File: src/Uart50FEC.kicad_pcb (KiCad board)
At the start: 2 copper layers, 24 x 27.9 mm, 23 parts, among them J1 105444-0001, J2 B4B-XH-A, U1 FT232RL, U2 MIC2005A-1

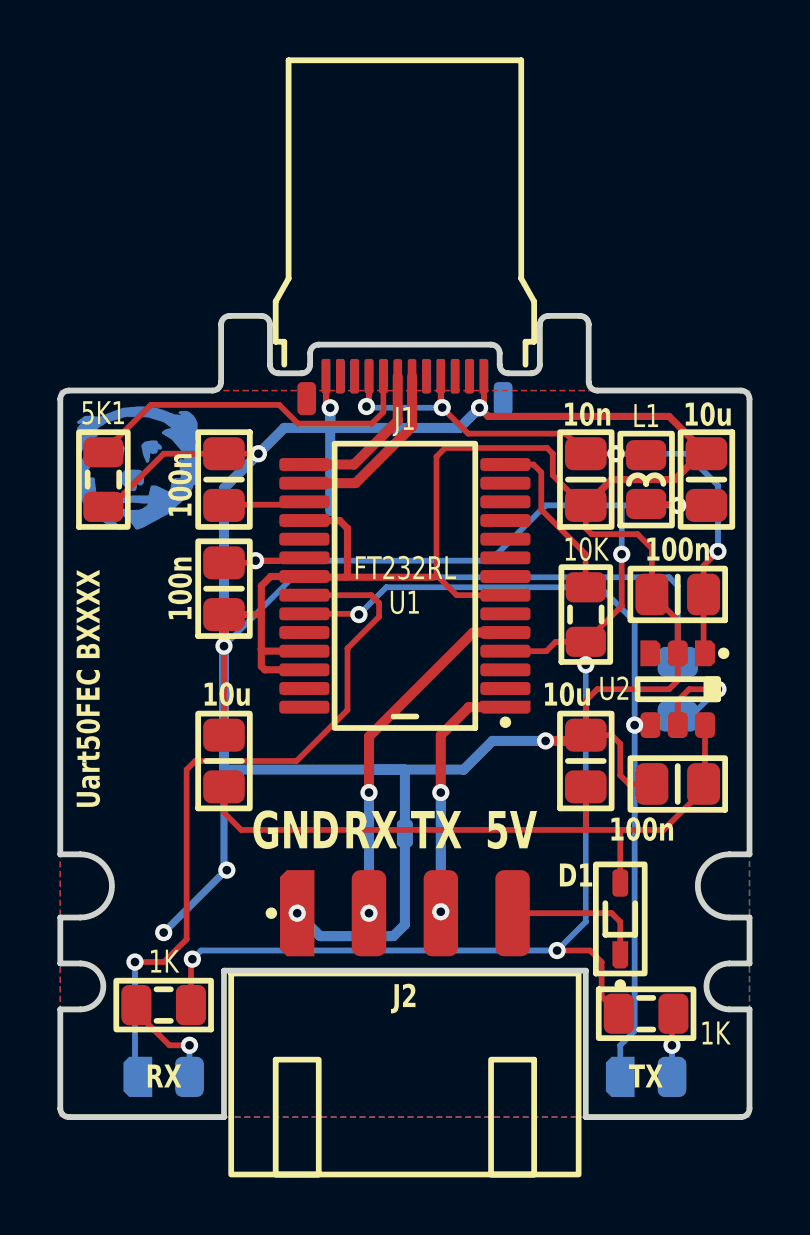
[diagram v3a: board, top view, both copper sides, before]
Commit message: Added jumper for always on
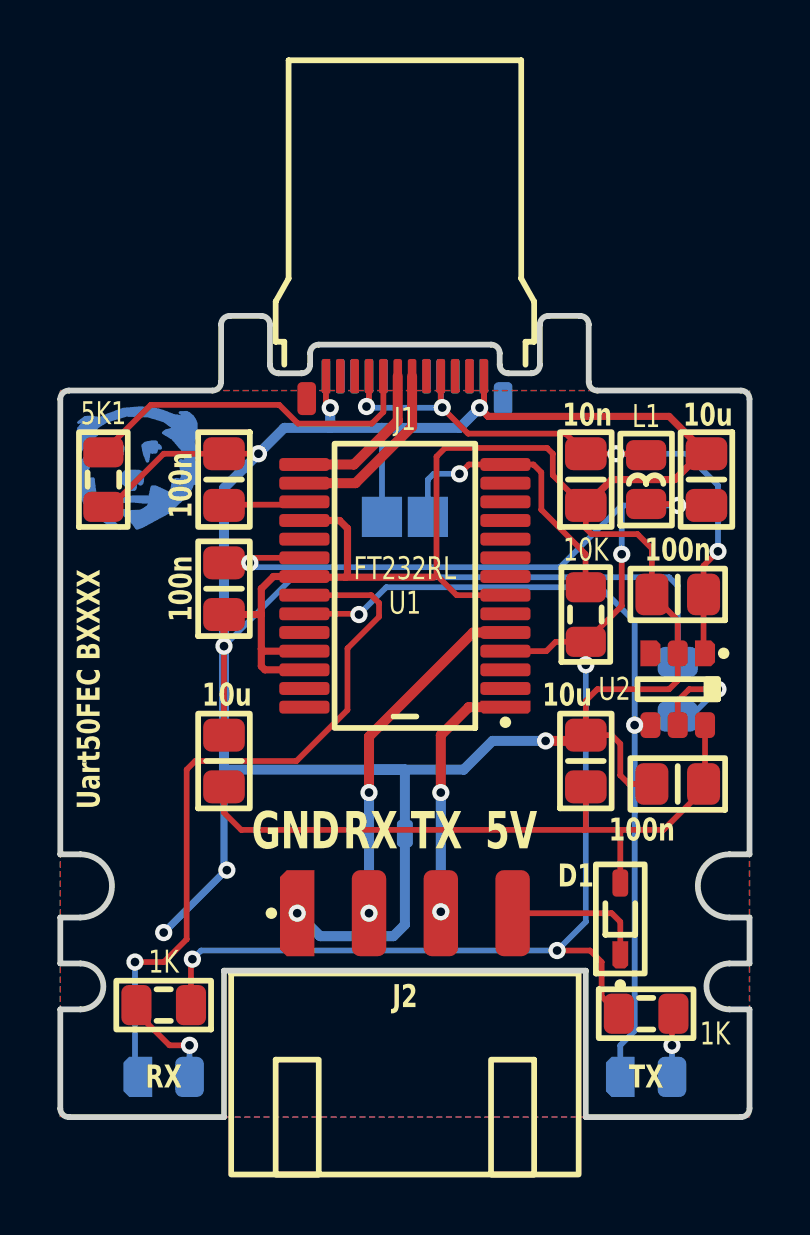
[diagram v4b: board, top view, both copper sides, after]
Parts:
- added JP1: ALWAYS ON, Medo64:JP (0805), B.Cu at (32.0, 27.0)
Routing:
- net PWREN#: track 6.00 -> 10.2 mm, vias 0 -> 1
- net GND: track 150.7 -> 150.2 mm
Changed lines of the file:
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@@
+		)
+	)
+	(footprint "Medo64:JP (0805)"
+		(layer "B.Cu")
+		(at 32 27 180)
+		(property "Reference" "JP1"
+			(at 0 1.5 180)
+			(layer "B.SilkS")
+			(hide yes)
+			(effects
+				(font
+					(size 0.8 0.6)
+					(thickness 0.15)
+					(bold yes)
+				)
+				(justify mirror)
+			)
+		)
+		(property "Value" "ALWAYS ON"
+			(at 0 -1.6 180)
+			(layer "B.SilkS")
+			(effects
+				(font
+					(size 0.8 0.6)
+					(thickness 0.15)
+					(bold yes)
+				)
+				(justify mirror)
+			)
+		)
+		(property "Footprint" "Medo64:JP (0805)"
+			(at 0 0 0)
+			(unlocked yes)
+			(layer "B.Fab")
+			(hide yes)
+			(effects
+				(font
+					(size 1.27 1.27)
+				)
+				(justify mirror)
+			)
+		)
+		(property "Datasheet" ""
+			(at 0 0 0)
+			(unlocked yes)
+			(layer "B.Fab")
+			(hide yes)
+			(effects
+				(font
+					(size 1.27 1.27)
+				)
+				(justify mirror)
+			)
+		)
+		(property "Description" ""
+			(at 0 0 0)
+			(unlocked yes)
+			(layer "B.Fab")
+			(hide yes)
+			(effects
+				(font
+					(size 1.27 1.27)
+				)
+				(justify mirror)
+			)
+		)
+		(attr smd)
+		(fp_rect
+			(start 1.65 -0.85)
+			(end -1.65 0.85)
+			(stroke
+				(width 0.2)
+				(type default)
+			)
+			(fill none)
+			(layer "B.SilkS")
+		)
+		(fp_rect
+			(start 0.1 -0.7)
+			(end -0.1 0.7)
+			(stroke
+				(width 0)
+				(type solid)
+			)
+			(fill solid)
+			(layer "B.Mask")
+		)
+		(fp_rect
+			(start 1.75 -0.95)
+			(end -1.75 0.95)
+			(stroke
+				(width 0.01)
+				(type dash)
+			)
+			(fill none)
+			(layer "B.CrtYd")
+		)
+		(pad "1" smd roundrect
+			(at -0.8 0 180)
+			(size 1.4 1.4)
+			(layers "B.Cu" "B.Mask")
+			(roundrect_rratio 0.5)
+			(chamfer_ratio 0)
+			(chamfer top_right bottom_right)
+			(net 10 "PWREN#")
+			(thermal_bridge_angle 45)
+		)
+		(pad "2" smd roundrect
+			(at 0.8 0 180)
+			(size 1.4 1.4)
+			(layers "B.Cu" "B.Mask")
+			(roundrect_rratio 0.5)
+			(chamfer_ratio 0)
+			(chamfer top_left bottom_left)
+			(net 7 "GND")
+			(thermal_bridge_angle 45)
 		)
 	)
@@
 	)
 	(segment
-		(start 28.5 28.525)
-		(end 26.8 28.525)
-		(width 0.2)
-		(layer "F.Cu")
-		(net 3)
-	)
-	(segment
-		(start 26.725 28.6)
-		(end 26.8 28.525)
+		(start 25.7 28.6)
+		(end 26.599996 28.6)
 		(width 0.2)
 		(layer "F.Cu")
@@
 	)
 	(segment
+		(start 26.774996 28.425)
+		(end 26.599996 28.6)
+		(width 0.2)
+		(layer "F.Cu")
+		(net 3)
+	)
+	(segment
 		(start 24.55 42.449998)
 		(end 24.599998 42.4)
@@
 	)
 	(segment
-		(start 25.7 28.6)
-		(end 26.725 28.6)
-		(width 0.2)
-		(layer "F.Cu")
-		(net 3)
-	)
-	(segment
 		(start 35.5 31.675)
 		(end 36.925 31.675)
@@
 	)
 	(segment
+		(start 28.5 28.425)
+		(end 26.774996 28.425)
+		(width 0.2)
+		(layer "F.Cu")
+		(net 3)
+	)
+	(segment
 		(start 38.3 31.35)
 		(end 39.55 30.1)
@@
 	)
 	(via
-		(at 26.8 28.525)
+		(at 26.599996 28.6)
 		(size 0.6)
 		(drill 0.3)
@@
 	)
 	(segment
+		(start 37.4 28.75)
+		(end 26.8 28.75)
+		(width 0.2)
+		(layer "B.Cu")
+		(net 3)
+	)
+	(segment
+		(start 26.8 28.75)
+		(end 26.65 28.6)
+		(width 0.2)
+		(layer "B.Cu")
+		(net 3)
+	)
+	(segment
 		(start 39.55 26.6)
 		(end 41.499994 26.6)
@@
 	)
 	(segment
-		(start 36.9 26.6)
-		(end 39.55 26.6)
+		(start 39.55 26.6)
+		(end 37.4 28.75)
 		(width 0.2)
 		(layer "B.Cu")
@@
 	)
 	(segment
-		(start 26.8 28.525)
-		(end 34.975 28.525)
-		(width 0.2)
-		(layer "B.Cu")
-		(net 3)
-	)
-	(segment
 		(start 24.599998 42.4)
 		(end 24.899998 42.1)
@@
 	)
 	(segment
-		(start 34.975 28.525)
-		(end 36.9 26.6)
+		(start 26.65 28.6)
+		(end 26.599996 28.6)
 		(width 0.2)
 		(layer "B.Cu")
@@
 	)
 	(segment
-		(start 27 29.4)
-		(end 27.325 29.075)
-		(width 0.25)
-		(layer "F.Cu")
-		(net 7)
-	)
-	(segment
 		(start 38.7 33)
 		(end 41.2 33)
@@
 	)
 	(segment
+		(start 27 30.4)
+		(end 27 29.5)
+		(width 0.25)
+		(layer "F.Cu")
+		(net 7)
+	)
+	(segment
 		(start 34.75 22.1)
 		(end 34.75 23.05)
@@
 	)
 	(segment
+		(start 27.425 29.075)
+		(end 28.5 29.075)
+		(width 0.25)
+		(layer "F.Cu")
+		(net 7)
+	)
+	(segment
 		(start 30 27.4)
 		(end 30 29.025)
@@
 	)
 	(segment
-		(start 27.325 29.075)
-		(end 28.5 29.075)
-		(width 0.25)
-		(layer "F.Cu")
-		(net 7)
-	)
-	(segment
 		(start 41.5 32.7)
 		(end 41.5 31.75)
@@
 	)
 	(segment
-		(start 27 30.4)
-		(end 27 29.4)
-		(width 0.25)
-		(layer "F.Cu")
-		(net 7)
-	)
-	(segment
 		(start 35.5 29.725)
 		(end 33.8 29.725)
@@
 		(start 29.725 27.125)
 		(end 30 27.4)
+		(width 0.25)
+		(layer "F.Cu")
+		(net 7)
+	)
+	(segment
+		(start 27 29.5)
+		(end 27.425 29.075)
 		(width 0.25)
 		(layer "F.Cu")
@@
 	)
 	(segment
+		(start 31.2 27)
+		(end 31.2 23.9)
+		(width 0.2)
+		(layer "B.Cu")
+		(net 7)
+	)
+	(segment
 		(start 41.2 29.1)
 		(end 28.1 29.1)
@@
 	)
 	(segment
+		(start 29.4 23.9)
+		(end 31.2 23.9)
+		(width 0.35)
+		(layer "B.Cu")
+		(net 7)
+	)
+	(segment
 		(start 34.75 22.1)
 		(end 34.75 23.05)
@@
 	)
 	(segment
-		(start 29.4 23.9)
-		(end 33.9 23.9)
-		(width 0.35)
-		(layer "B.Cu")
-		(net 7)
-	)
-	(segment
 		(start 32 41.2)
 		(end 31.6 41.6)
@@
 	)
 	(segment
-		(start 29.4 26.8)
-		(end 29.4 23.2)
-		(width 0.35)
-		(layer "B.Cu")
-		(net 7)
-	)
-	(segment
 		(start 32 35.8)
 		(end 32 38.025)
+		(width 0.35)
+		(layer "B.Cu")
+		(net 7)
+	)
+	(segment
+		(start 31.2 23.9)
+		(end 33.9 23.9)
 		(width 0.35)
 		(layer "B.Cu")
@@
 	)
 	(segment
+		(start 34.225 25.175)
+		(end 33.9 25.5)
+		(width 0.2)
+		(layer "F.Cu")
+		(net 10)
+	)
+	(segment
 		(start 38.29 29.45)
 		(end 38.29 28.29)
@@
 		(net 10)
 	)
+	(segment
+		(start 35.5 25.175)
+		(end 34.225 25.175)
+		(width 0.2)
+		(layer "F.Cu")
+		(net 10)
+	)
+	(via
+		(at 33.9 25.5)
+		(size 0.6)
+		(drill 0.3)
+		(layers "F.Cu" "B.Cu")
+		(net 10)
+	)
+	(segment
+		(start 32.8 27)
+		(end 32.8 25.7)
+		(width 0.2)
+		(layer "B.Cu")
+		(net 10)
+	)
+	(segment
+		(start 32.8 25.7)
+		(end 33 25.5)
+		(width 0.2)
+		(layer "B.Cu")
+		(net 10)
+	)
+	(segment
+		(start 33 25.5)
+		(end 33.9 25.5)
+		(width 0.2)
+		(layer "B.Cu")
+		(net 10)
+	)

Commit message: Lowering output current a bit
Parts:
- R5: value 68K -> 75K
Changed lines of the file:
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@@
 			)
 		)
-		(property "Value" "68K"
+		(property "Value" "75K"
 			(at 2.25 0 0)
 			(layer "B.SilkS")

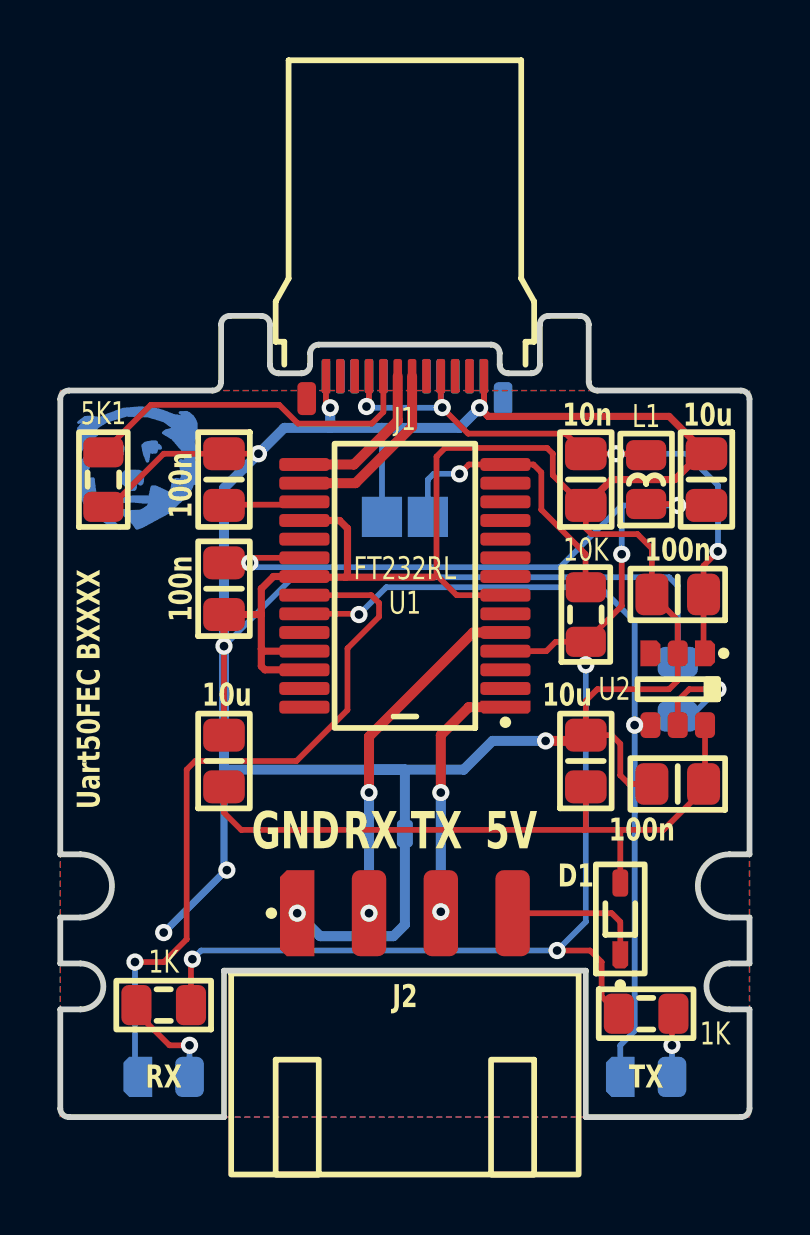
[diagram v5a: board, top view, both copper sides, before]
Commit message: Fixed output enable
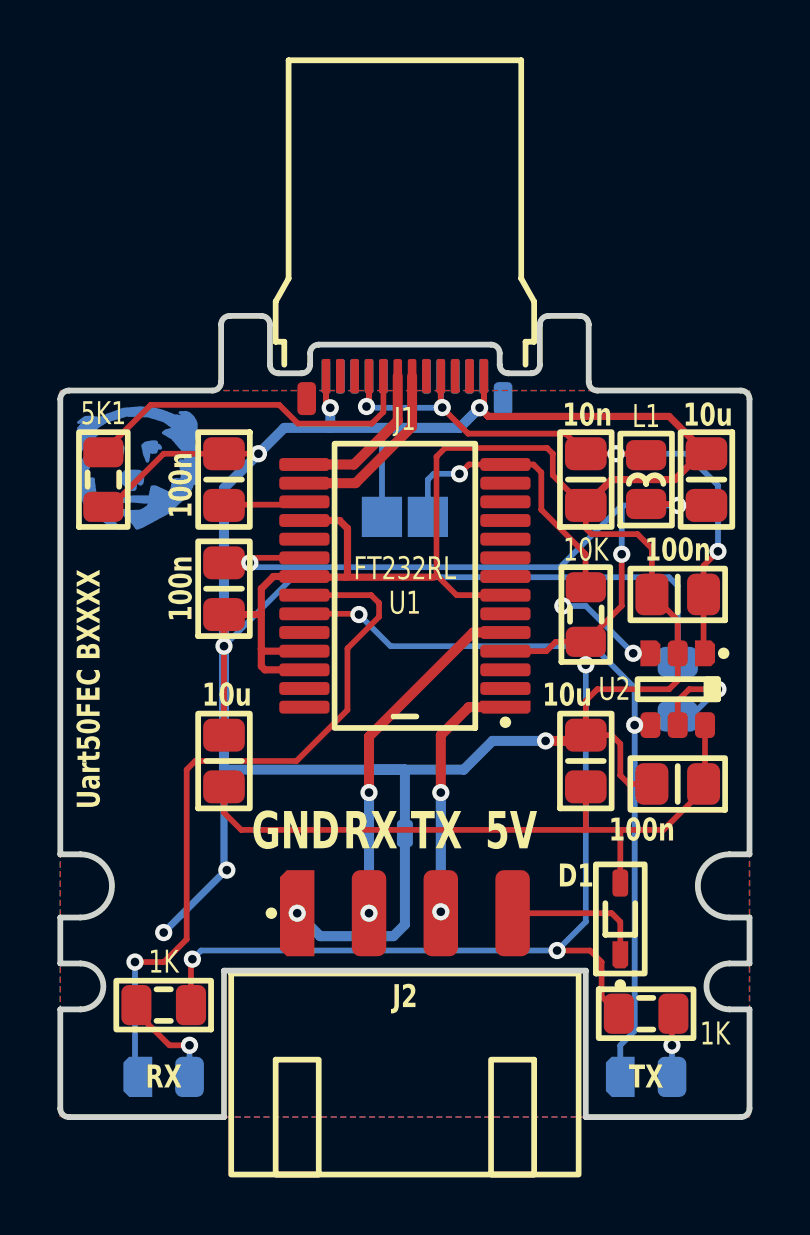
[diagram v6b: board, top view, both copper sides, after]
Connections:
- net 3V3usb renamed 3V3_UART_USB
- net OUT_5V renamed 5V_OUT'
- net OUT_V+ renamed 5V_OUT
- net USB_5V renamed 5V_USB
- U2 pad 3: 5V_SW -> PWREN#
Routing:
- net PWREN#: track 10.2 -> 15.0 mm, vias 1 -> 3
- net LED_TX#: track 29.0 -> 26.9 mm

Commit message: Updated net names
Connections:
- net 5V_OUT' renamed 5V_SWITCHED
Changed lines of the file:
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@@
 	(net 15 "5V_USB")
 	(net 16 "5V_OUT")
-	(net 17 "5V_OUT'")
+	(net 17 "5V_SWITCHED")
 	(footprint "Medo64:R (0805)"
 		(layer "F.Cu")
@@
 			(layers "F.Cu" "F.Paste" "F.Mask")
 			(roundrect_rratio 0.25)
-			(net 17 "5V_OUT'")
+			(net 17 "5V_SWITCHED")
 			(thermal_bridge_angle 45)
 		)
@@
 			(layers "F.Cu" "F.Paste" "F.Mask")
 			(roundrect_rratio 0.25)
-			(net 17 "5V_OUT'")
+			(net 17 "5V_SWITCHED")
 			(thermal_bridge_angle 45)
 		)
@@
 			(layers "F.Cu" "F.Paste" "F.Mask")
 			(roundrect_rratio 0.25)
-			(net 17 "5V_OUT'")
+			(net 17 "5V_SWITCHED")
 			(thermal_bridge_angle 45)
 		)
@@
 			(layers "F.Cu" "F.Paste" "F.Mask")
 			(roundrect_rratio 0.25)
-			(net 17 "5V_OUT'")
+			(net 17 "5V_SWITCHED")
 			(thermal_bridge_angle 45)
 		)
@@
 			(layers "F.Cu" "F.Paste" "F.Mask")
 			(roundrect_rratio 0.25)
-			(net 17 "5V_OUT'")
+			(net 17 "5V_SWITCHED")
 			(thermal_bridge_angle 45)
 		)
